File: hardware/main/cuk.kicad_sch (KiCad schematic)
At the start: 62 parts, among them Q401 BSC093N15NS5, Q402 BSC093N15NS5

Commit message: Schematics: Anotate testpoints
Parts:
- gave numbers to parts that had none: 4
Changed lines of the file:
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@@
   (symbol (lib_id "Connector:TestPoint") (at 170.18 179.07 0) (unit 1)
     (in_bom yes) (on_board yes) (fields_autoplaced)
-    (property "Reference" "TP?" (id 0) (at 171.577 174.9333 0)
+    (property "Reference" "TP406" (id 0) (at 171.577 174.9333 0)
       (effects (font (size 1.27 1.27)) (justify left))
     )
@@
   (symbol (lib_id "Connector:TestPoint") (at 170.18 163.195 0) (unit 1)
     (in_bom yes) (on_board yes) (fields_autoplaced)
-    (property "Reference" "TP?" (id 0) (at 171.577 159.0583 0)
+    (property "Reference" "TP404" (id 0) (at 171.577 159.0583 0)
       (effects (font (size 1.27 1.27)) (justify left))
     )
@@
   (symbol (lib_id "Connector:TestPoint") (at 170.18 170.815 0) (unit 1)
     (in_bom yes) (on_board yes) (fields_autoplaced)
-    (property "Reference" "TP?" (id 0) (at 171.577 166.6783 0)
+    (property "Reference" "TP405" (id 0) (at 171.577 166.6783 0)
       (effects (font (size 1.27 1.27)) (justify left))
     )
@@
   (symbol (lib_id "Connector:TestPoint") (at 170.18 154.94 0) (unit 1)
     (in_bom yes) (on_board yes) (fields_autoplaced)
-    (property "Reference" "TP?" (id 0) (at 171.577 150.8033 0)
-      (effects (font (size 1.27 1.27)) (justify left))
-    )
+    (property "Reference" "TP403" (id 0) (at 171.577 150.8033 0)
+      (effects (font (size 1.27 1.27)) (justify left))
+    )

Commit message: Layout: Designing thermal dissipation and optimizing control
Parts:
- added HS401: HS10334, Zenite:HS10334 60mmx17mm, symbol Mechanical:Heatsink
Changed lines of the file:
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@@
     (pin "2")
+  )
+  (symbol (lib_id "Mechanical:Heatsink") (at 65.405 80.01 0) (unit 1)
+    (in_bom yes) (on_board yes) (fields_autoplaced)
+    (property "Reference" "HS401" (id 0) (at 69.0118 77.2703 0)
+      (effects (font (size 1.27 1.27)) (justify left))
+    )
+    (property "Value" "HS10334" (id 1) (at 69.0118 79.8072 0)
+      (effects (font (size 1.27 1.27)) (justify left))
+    )
+    (property "Footprint" "Zenite:HS10334 60mmx17mm" (id 2) (at 65.7098 80.01 0)
+      (effects (font (size 1.27 1.27)) hide)
+    )
+    (property "Datasheet" "~" (id 3) (at 65.7098 80.01 0)
+      (effects (font (size 1.27 1.27)) hide)
+    )
   )
   (symbol (lib_id "Device:D_Schottky_AAK") (at 164.465 116.205 270) (unit 1)

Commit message: Layout: Connect all unconected nets, and fix all DRC errors
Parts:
- added R401: 10kR 0805, Resistor_SMD:R_0805_2012Metric_Pad1.20x1.40mm_HandSolder, symbol Device:R_Small
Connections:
- net S: now also R401.1
- net driver/OUT_G: now also R401.2
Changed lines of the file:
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@@
   (junction (at 173.355 50.8) (diameter 0) (color 0 0 0 0)
   )
+  (junction (at 97.79 153.67) (diameter 0) (color 0 0 0 0)
+  )
   (junction (at 66.04 34.29) (diameter 0) (color 0 0 0 0)
   )
@@
   (junction (at 87.63 41.275) (diameter 0) (color 0 0 0 0)
   )
+  (junction (at 97.79 162.56) (diameter 0) (color 0 0 0 0)
+  )
   (junction (at 192.405 119.38) (diameter 0) (color 0 0 0 0)
   )
@@
     (stroke (width 0) (type default) (color 0 0 0 0))
   )
+  (wire (pts (xy 97.79 155.575) (xy 97.79 153.67))
+    (stroke (width 0) (type default) (color 0 0 0 0))
+  )
   (polyline (pts (xy 120.65 58.42) (xy 22.225 58.42))
     (stroke (width 0) (type default) (color 0 0 0 0))
@@
     (stroke (width 0) (type default) (color 0 0 0 0))
   )
+  (wire (pts (xy 97.79 162.56) (xy 113.03 162.56))
+    (stroke (width 0) (type default) (color 0 0 0 0))
+  )
   (wire (pts (xy 203.835 114.3) (xy 207.645 114.3))
     (stroke (width 0) (type default) (color 0 0 0 0))
@@
     (stroke (width 0) (type default) (color 0 0 0 0))
   )
-  (wire (pts (xy 98.425 156.21) (xy 98.425 162.56))
+  (wire (pts (xy 93.345 156.21) (xy 93.345 162.56))
     (stroke (width 0) (type default) (color 0 0 0 0))
   )
@@
     (stroke (width 0) (type default) (color 0 0 0 0))
   )
-  (wire (pts (xy 98.425 162.56) (xy 113.03 162.56))
+  (wire (pts (xy 93.345 162.56) (xy 97.79 162.56))
     (stroke (width 0) (type default) (color 0 0 0 0))
   )
@@
     (stroke (width 0) (type default) (color 0 0 0 0))
   )
+  (wire (pts (xy 97.79 153.67) (xy 104.14 153.67))
+    (stroke (width 0) (type default) (color 0 0 0 0))
+  )
   (wire (pts (xy 164.465 100.33) (xy 171.45 100.33))
     (stroke (width 0) (type default) (color 0 0 0 0))
@@
     (stroke (width 0) (type default) (color 0 0 0 0))
   )
+  (wire (pts (xy 97.79 160.655) (xy 97.79 162.56))
+    (stroke (width 0) (type default) (color 0 0 0 0))
+  )
   (wire (pts (xy 200.025 114.3) (xy 203.835 114.3))
     (stroke (width 0) (type default) (color 0 0 0 0))
@@
     (stroke (width 0) (type default) (color 0 0 0 0))
   )
-  (wire (pts (xy 86.995 153.67) (xy 104.14 153.67))
+  (wire (pts (xy 86.995 153.67) (xy 97.79 153.67))
     (stroke (width 0) (type default) (color 0 0 0 0))
   )
@@
     (stroke (width 0) (type default) (color 0 0 0 0))
   )
-  (wire (pts (xy 86.995 156.21) (xy 98.425 156.21))
+  (wire (pts (xy 86.995 156.21) (xy 93.345 156.21))
     (stroke (width 0) (type default) (color 0 0 0 0))
   )
@@
       (effects (font (size 1.27 1.27)) hide)
     )
+    (pin "1")
+    (pin "2")
+  )
+  (symbol (lib_id "Device:R_Small") (at 97.79 158.115 180) (unit 1)
+    (in_bom yes) (on_board yes) (fields_autoplaced)
+    (property "Reference" "R401" (id 0) (at 99.2886 157.2803 0)
+      (effects (font (size 1.27 1.27)) (justify right))
+    )
+    (property "Value" "10kR 0805" (id 1) (at 99.2886 159.8172 0)
+      (effects (font (size 1.27 1.27)) (justify right))
+    )
+    (property "Footprint" "Resistor_SMD:R_0805_2012Metric_Pad1.20x1.40mm_HandSolder" (id 2) (at 97.79 158.115 0)
+      (effects (font (size 1.27 1.27)) hide)
+    )
+    (property "Datasheet" "~" (id 3) (at 97.79 158.115 0)
+      (effects (font (size 1.27 1.27)) hide)
+    )

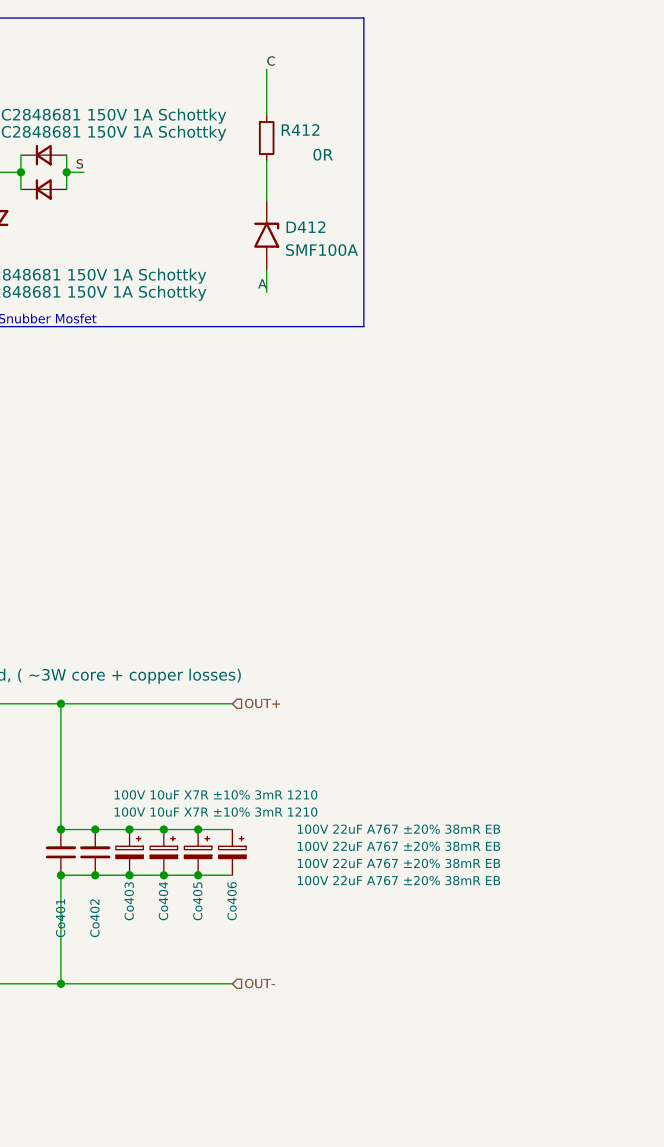
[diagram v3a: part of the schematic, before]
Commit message: layout: Separating analogical power nets
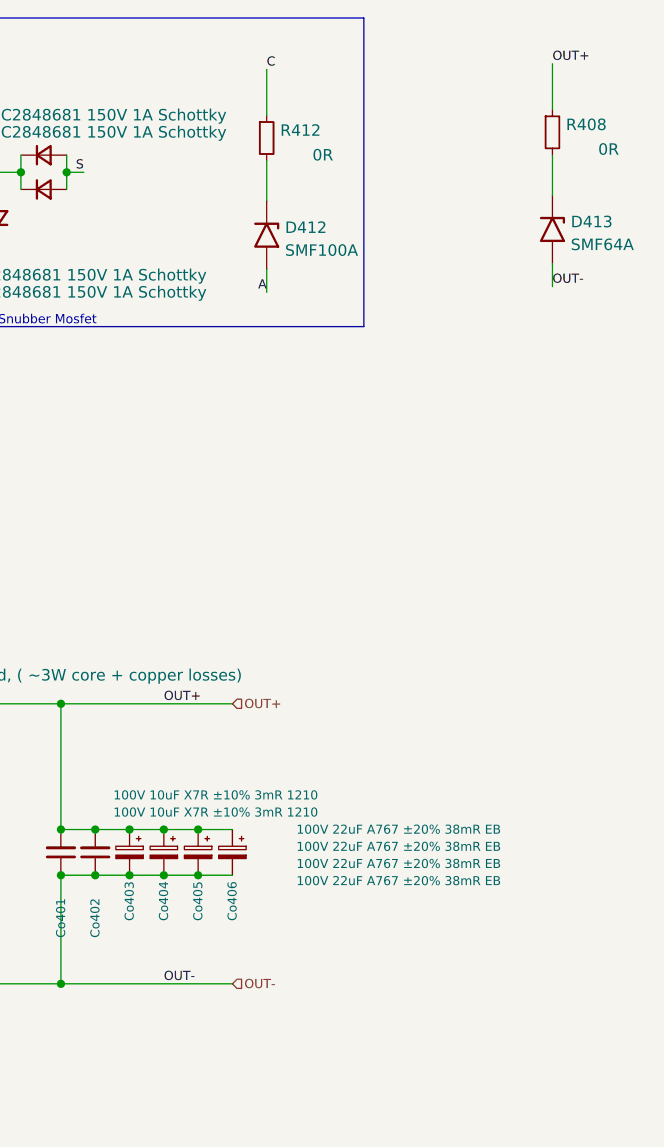
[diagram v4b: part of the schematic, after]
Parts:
- added D413: SMF64A, Diode_SMD:D_SOD-123F, symbol Diode:SMF18A
- added R408: 0R, Resistor_SMD:R_0805_2012Metric_Pad1.20x1.40mm_HandSolder, symbol Device:R_Small
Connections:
- net IN+: now also D413.2 (A2)
- net OUT+: now also R408.1
- new net: D413.1 (A1), R408.2
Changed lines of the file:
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@@
+    (stroke (width 0) (type default) (color 0 0 0 0))
+  )
+  (wire (pts (xy 247.015 51.435) (xy 247.015 53.975))
     (stroke (width 0) (type default) (color 0 0 0 0))
   )
@@
     (stroke (width 0) (type default) (color 0 0 0 0))
   )
+  (wire (pts (xy 247.015 39.37) (xy 247.015 43.815))
+    (stroke (width 0) (type default) (color 0 0 0 0))
+  )
   (wire (pts (xy 64.135 41.275) (xy 64.135 39.37))
     (stroke (width 0) (type default) (color 0 0 0 0))
@@
     (stroke (width 0) (type default) (color 0 0 0 0))
   )
+  (wire (pts (xy 247.015 29.21) (xy 247.015 34.29))
+    (stroke (width 0) (type default) (color 0 0 0 0))
+  )
   (wire (pts (xy 160.02 170.815) (xy 170.18 170.815))
     (stroke (width 0) (type default) (color 0 0 0 0))
@@
     (effects (font (size 1.016 1.016)) (justify right bottom))
   )
+  (label "OUT+" (at 203.835 100.33 0)
+    (effects (font (size 1.016 1.016)) (justify left bottom))
+  )
   (label "A" (at 159.385 122.555 270)
     (effects (font (size 1.016 1.016)) (justify right bottom))
@@
     (effects (font (size 1.016 1.016)) (justify right bottom))
   )
+  (label "OUT+" (at 247.015 29.21 0)
+    (effects (font (size 1.016 1.016)) (justify left bottom))
+  )
   (label "G0" (at 116.84 116.205 0)
     (effects (font (size 1.016 1.016)) (justify left bottom))
@@
     (effects (font (size 1.016 1.016)) (justify left bottom))
   )
+  (label "OUT-" (at 247.015 53.975 0)
+    (effects (font (size 1.016 1.016)) (justify left bottom))
+  )
   (label "D" (at 127 121.92 270)
     (effects (font (size 1.016 1.016)) (justify right bottom))
@@
   )
   (label "G0" (at 113.03 149.86 0)
+    (effects (font (size 1.016 1.016)) (justify left bottom))
+  )
+  (label "OUT-" (at 203.835 131.445 0)
     (effects (font (size 1.016 1.016)) (justify left bottom))
   )
@@
     (pin "2")
   )
+  (symbol (lib_id "Diode:SMF18A") (at 247.015 47.625 270) (unit 1)
+    (in_bom yes) (on_board yes) (fields_autoplaced)
+    (property "Reference" "D413" (id 0) (at 249.047 46.7903 90)
+      (effects (font (size 1.27 1.27)) (justify left))
+    )
+    (property "Value" "SMF64A" (id 1) (at 249.047 49.3272 90)
+      (effects (font (size 1.27 1.27)) (justify left))
+    )
+    (property "Footprint" "Diode_SMD:D_SOD-123F" (id 2) (at 241.935 47.625 0)
+      (effects (font (size 1.27 1.27)) hide)
+    )
+    (property "Datasheet" "https://datasheet.lcsc.com/lcsc/2104161903_Shandong-Jingdao-Microelectronics-SMF100A_C169441.pdf" (id 3) (at 247.015 46.355 0)
+      (effects (font (size 1.27 1.27)) hide)
+    )
+    (pin "1")
+    (pin "2")
+  )
   (symbol (lib_id "Diode:SMF18A") (at 109.22 46.99 270) (unit 1)
     (in_bom yes) (on_board yes) (fields_autoplaced)
@@
       (effects (font (size 1.27 1.27)) hide)
     )
+    (pin "1")
+    (pin "2")
+  )
+  (symbol (lib_id "Device:R_Small") (at 247.015 36.83 0) (unit 1)
+    (in_bom yes) (on_board yes)
+    (property "Reference" "R408" (id 0) (at 248.5136 35.9953 0)
+      (effects (font (size 1.27 1.27)) (justify left))
+    )
+    (property "Value" "0R" (id 1) (at 252.095 38.735 0)
+      (effects (font (size 1.27 1.27)) (justify left))
+    )
+    (property "Footprint" "Resistor_SMD:R_0805_2012Metric_Pad1.20x1.40mm_HandSolder" (id 2) (at 247.015 36.83 0)
+      (effects (font (size 1.27 1.27)) hide)
+    )
+    (property "Datasheet" "~" (id 3) (at 247.015 36.83 0)
+      (effects (font (size 1.27 1.27)) hide)
+    )

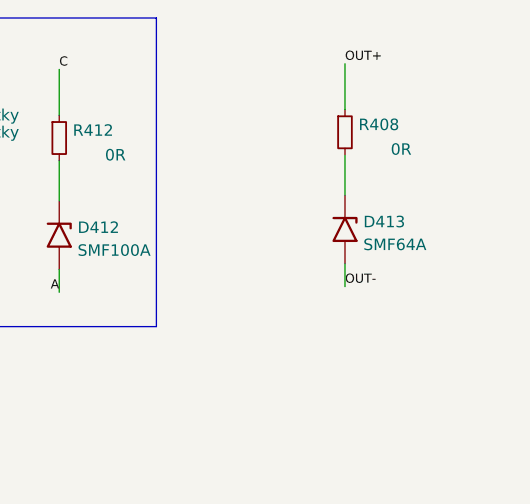
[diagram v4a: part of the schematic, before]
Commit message: Layout: Finalize first vesion of control (DRC ok) and modify vias for better via density
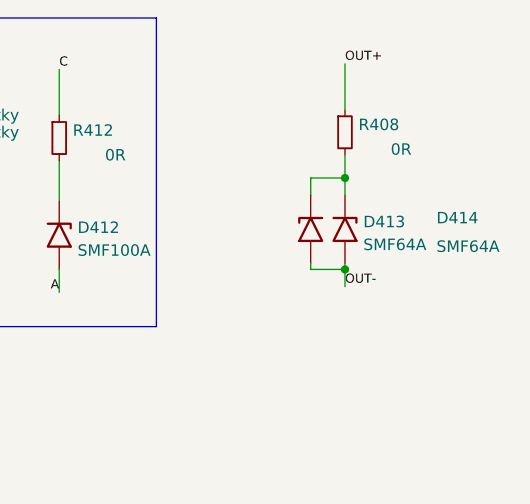
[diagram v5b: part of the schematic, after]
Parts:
- added D414: SMF64A, Diode_SMD:D_SOD-123F, symbol Diode:SMF18A
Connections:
- net IN+: now also D414.2 (A2)
- net at D413.1 (A1), R408.2: now also D414.1 (A1)
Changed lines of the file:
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@@
   (junction (at 187.96 41.275) (diameter 0) (color 0 0 0 0)
   )
+  (junction (at 247.015 52.07) (diameter 0) (color 0 0 0 0)
+  )
   (junction (at 91.44 113.665) (diameter 0) (color 0 0 0 0)
   )
@@
   (junction (at 87.63 113.665) (diameter 0) (color 0 0 0 0)
   )
+  (junction (at 247.015 41.91) (diameter 0) (color 0 0 0 0)
+  )
   (junction (at 151.765 87.63) (diameter 0) (color 0 0 0 0)
   )
@@
     (stroke (width 0) (type default) (color 0 0 0 0))
   )
+  (wire (pts (xy 247.015 41.91) (xy 247.015 43.815))
+    (stroke (width 0) (type default) (color 0 0 0 0))
+  )
   (wire (pts (xy 116.84 100.33) (xy 127 100.33))
     (stroke (width 0) (type default) (color 0 0 0 0))
   )
+  (wire (pts (xy 243.205 52.07) (xy 247.015 52.07))
+    (stroke (width 0) (type default) (color 0 0 0 0))
+  )
   (wire (pts (xy 83.82 100.33) (xy 99.06 100.33))
     (stroke (width 0) (type default) (color 0 0 0 0))
@@
     (stroke (width 0) (type default) (color 0 0 0 0))
   )
+  (wire (pts (xy 243.205 51.435) (xy 243.205 52.07))
+    (stroke (width 0) (type default) (color 0 0 0 0))
+  )
   (wire (pts (xy 97.79 160.655) (xy 97.79 162.56))
     (stroke (width 0) (type default) (color 0 0 0 0))
@@
     (stroke (width 0) (type default) (color 0 0 0 0))
   )
+  (wire (pts (xy 243.205 43.815) (xy 243.205 41.91))
+    (stroke (width 0) (type default) (color 0 0 0 0))
+  )
   (wire (pts (xy 91.44 118.745) (xy 95.25 118.745))
     (stroke (width 0) (type default) (color 0 0 0 0))
@@
     (stroke (width 0) (type default) (color 0 0 0 0))
   )
-  (wire (pts (xy 247.015 51.435) (xy 247.015 53.975))
+  (wire (pts (xy 247.015 51.435) (xy 247.015 52.07))
     (stroke (width 0) (type default) (color 0 0 0 0))
   )
@@
     (stroke (width 0) (type default) (color 0 0 0 0))
   )
-  (wire (pts (xy 247.015 39.37) (xy 247.015 43.815))
+  (wire (pts (xy 247.015 39.37) (xy 247.015 41.91))
     (stroke (width 0) (type default) (color 0 0 0 0))
   )
@@
     (stroke (width 0) (type default) (color 0 0 0 0))
   )
+  (wire (pts (xy 247.015 52.07) (xy 247.015 53.975))
+    (stroke (width 0) (type default) (color 0 0 0 0))
+  )
   (wire (pts (xy 127 100.33) (xy 127 111.125))
     (stroke (width 0) (type default) (color 0 0 0 0))
@@
   )
   (wire (pts (xy 193.04 41.275) (xy 193.04 43.18))
+    (stroke (width 0) (type default) (color 0 0 0 0))
+  )
+  (wire (pts (xy 243.205 41.91) (xy 247.015 41.91))
     (stroke (width 0) (type default) (color 0 0 0 0))
   )
@@
       (effects (font (size 1.27 1.27)) hide)
     )
+    (pin "1")
+    (pin "2")
+  )
+  (symbol (lib_id "Diode:SMF18A") (at 243.205 47.625 90) (mirror x) (unit 1)
+    (in_bom yes) (on_board yes)
+    (property "Reference" "D414" (id 0) (at 257.175 46.355 90)
+      (effects (font (size 1.27 1.27)) (justify right))
+    )
+    (property "Value" "SMF64A" (id 1) (at 257.175 49.53 90)
+      (effects (font (size 1.27 1.27)) (justify right))
+    )
+    (property "Footprint" "Diode_SMD:D_SOD-123F" (id 2) (at 248.285 47.625 0)
+      (effects (font (size 1.27 1.27)) hide)
+    )
+    (property "Datasheet" "https://datasheet.lcsc.com/lcsc/2104161903_Shandong-Jingdao-Microelectronics-SMF100A_C169441.pdf" (id 3) (at 243.205 46.355 0)
+      (effects (font (size 1.27 1.27)) hide)
+    )
